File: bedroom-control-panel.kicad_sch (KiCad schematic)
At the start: 33 parts, among them IC1 TLV1117-33CDCYG3, J1 USB4105-GF-A, U1 ESP32-S3-WROOM-1-N8R8, U2 PEC11L-4315F-S0009

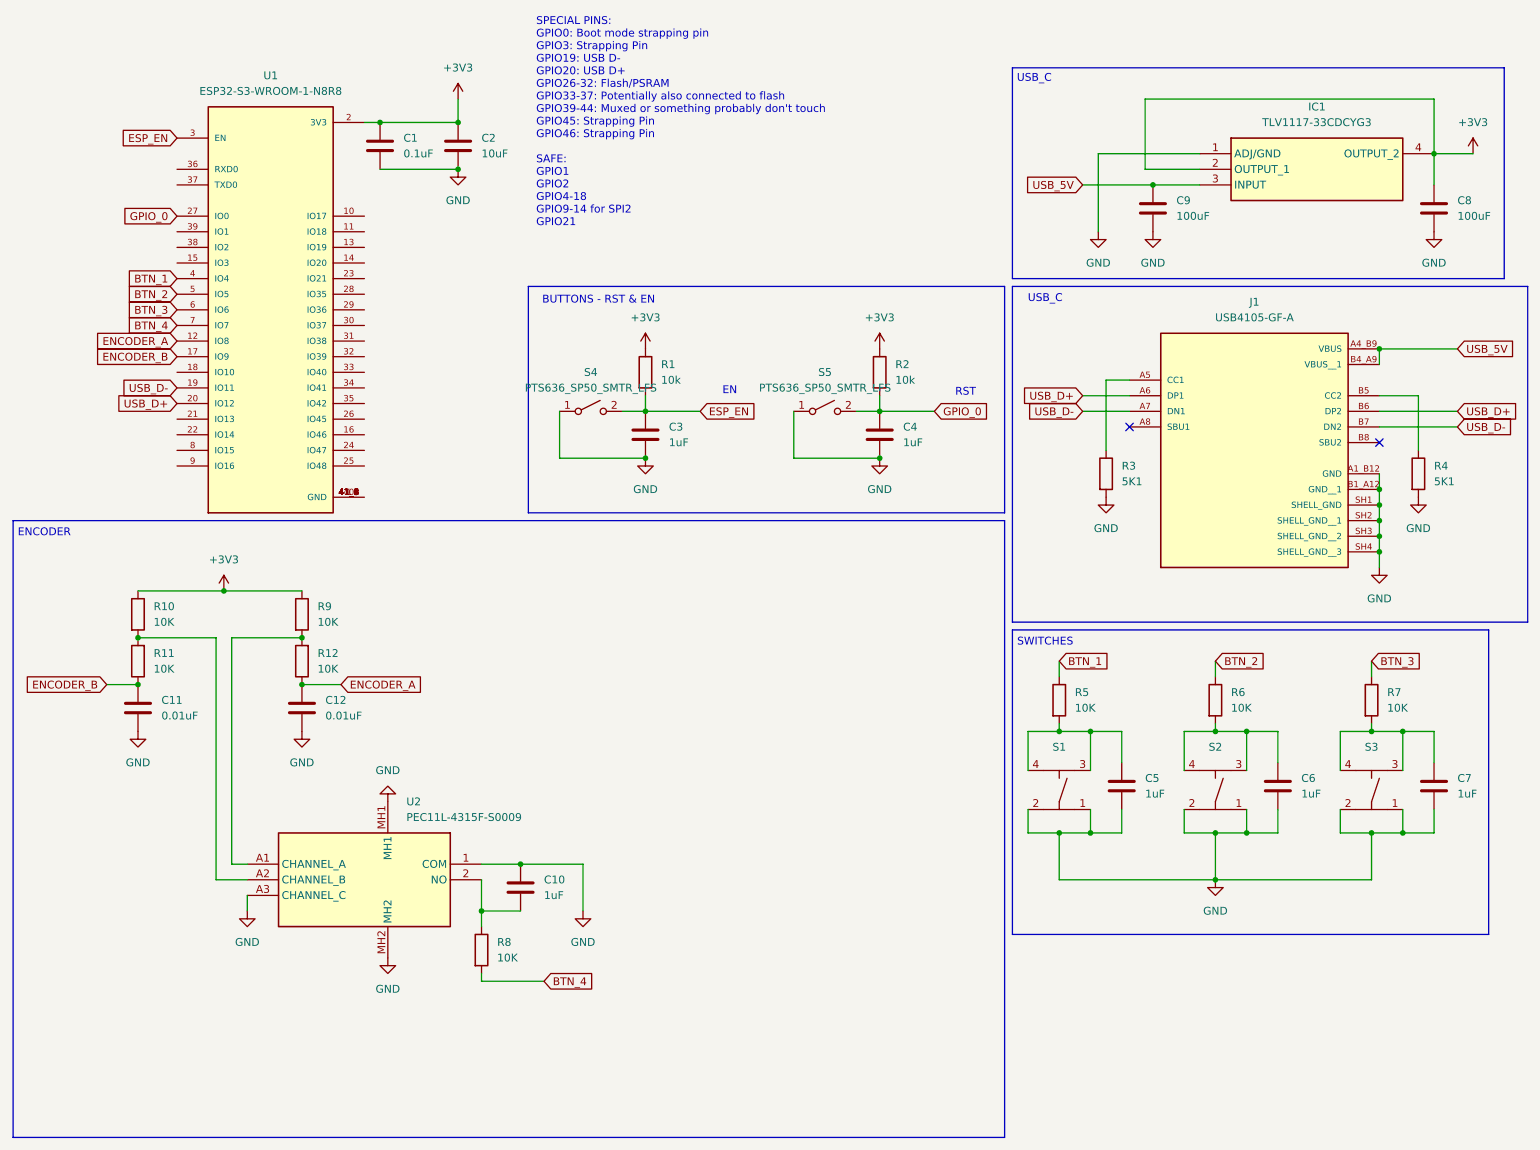
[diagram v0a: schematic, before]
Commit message: schematic complete, added bme680
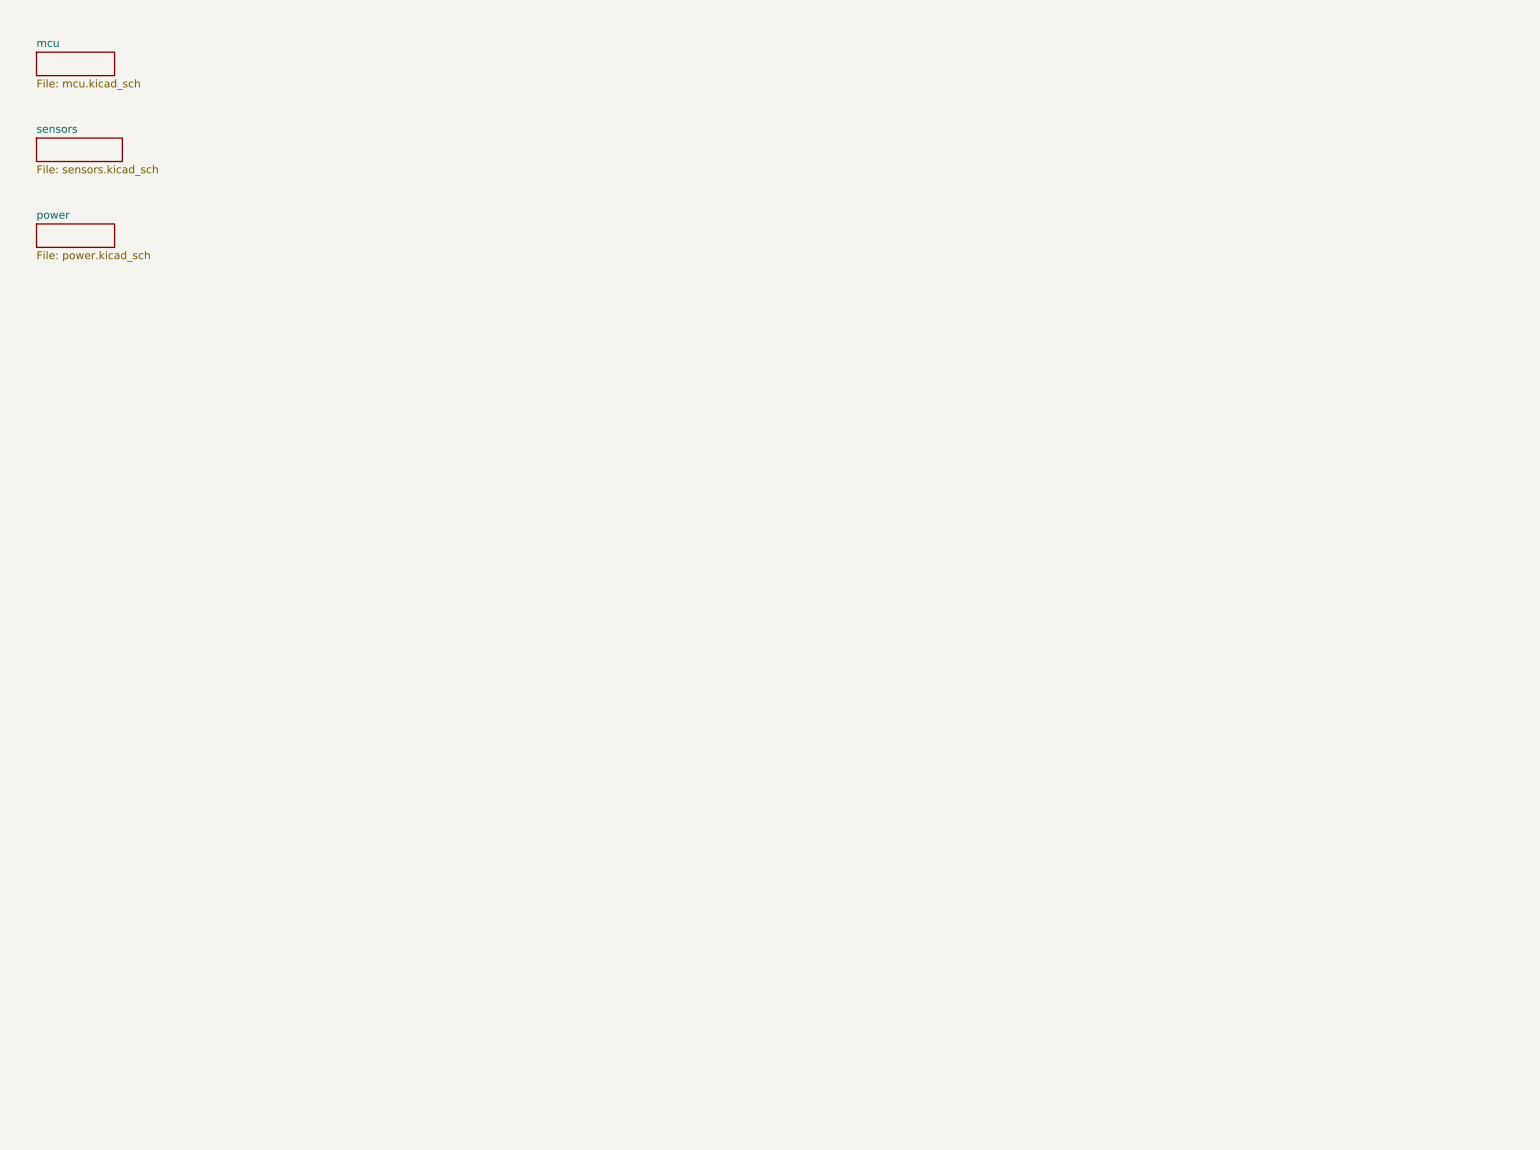
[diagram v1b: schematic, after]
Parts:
- removed C1: 0.1uF, Capacitor_SMD:C_1206_3216Metric, symbol Device:C
- removed C10, C3, C4, C5, C6, C7: 1uF, Capacitor_SMD:C_1206_3216Metric, symbol Device:C
- removed C11, C12: 0.01uF, Capacitor_SMD:C_1206_3216Metric, symbol Device:C
- removed C2: 10uF, Capacitor_SMD:C_1206_3216Metric, symbol Device:C
- removed C8, C9: 100uF, Capacitor_SMD:C_1206_3216Metric, symbol Device:C
- removed IC1: TLV1117-33CDCYG3, Samacsys:SOT230P700X180-4N, symbol Samacsys:TLV1117-33CDCYG3
- removed J1: USB4105-GF-A, Snapeda:USB4105-GF-A_GCT_USB4105-GF-A, symbol Snapeda:USB4105-GF-A
- removed R1, R2: 10k, Resistor_SMD:R_1206_3216Metric_Pad1.30x1.75mm_HandSolder, symbol Device:R
- removed R10, R11, R12, R5, R6, R7, R8, R9: 10K, Resistor_SMD:R_1206_3216Metric_Pad1.30x1.75mm_HandSolder, symbol Device:R
- removed R3, R4: 5K1, Resistor_SMD:R_1206_3216Metric_Pad1.30x1.75mm_HandSolder, symbol Device:R
- removed S1, S2, S3: ~, SamacSys_Parts:B3FS-1050, symbol SamacSys_Parts:OMRON_B3FS_Tactile_Switch
- removed S4, S5: PTS636_SP50_SMTR_LFS, SamacSys_Parts:PTS636SP50SMTRLFS, symbol Switch:SW_SPST
- removed U1: ESP32-S3-WROOM-1-N8R8, Snapeda:ESP32-S3-WROOM-1-N8R8_XCVR_ESP32S3WROOM1N8R8, symbol Snapeda:ESP32-S3-WROOM-1-N8R8
- removed U2: PEC11L-4315F-S0009, SamacSys_Parts:PEC11L4315FS0009, symbol SamacSys_Parts:PEC11L-4315F-S0009
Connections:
- no-connect marks 2 -> 0
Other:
- added sheet mcu (mcu.kicad_sch)
- added sheet power (power.kicad_sch)
- added sheet sensors (sensors.kicad_sch)
- note removed: "BUTTONS - RST & EN"
- note removed: "EN"
- note removed: "ENCODER"
- note removed: "RST"
- note removed: "SPECIAL PINS: GPIO0: Boot mode strapping pin GPIO3: Strapping Pin GPIO19: USB D- GPIO20: USB D+ GPIO26-32: Flash/PSRAM GPIO33-37: Potentially also connected to flash GPIO39-44: Muxed or something probably don't touch GPIO45: Strapping Pin GPIO46: Strapping Pin SAFE: GPIO1 GPIO2 GPIO4-18 GPIO9-14 for SPI2 GPIO21"
- note removed: "SWITCHES"
- note removed: "USB_C"
